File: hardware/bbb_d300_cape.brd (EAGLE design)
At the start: 58.4 x 54.6 mm, 38 parts, among them IC1 7414D, IC2 7414D, T1 2N3904, T2 2N3904, T3 2N3904, T4 2N3904, T5 2N3904

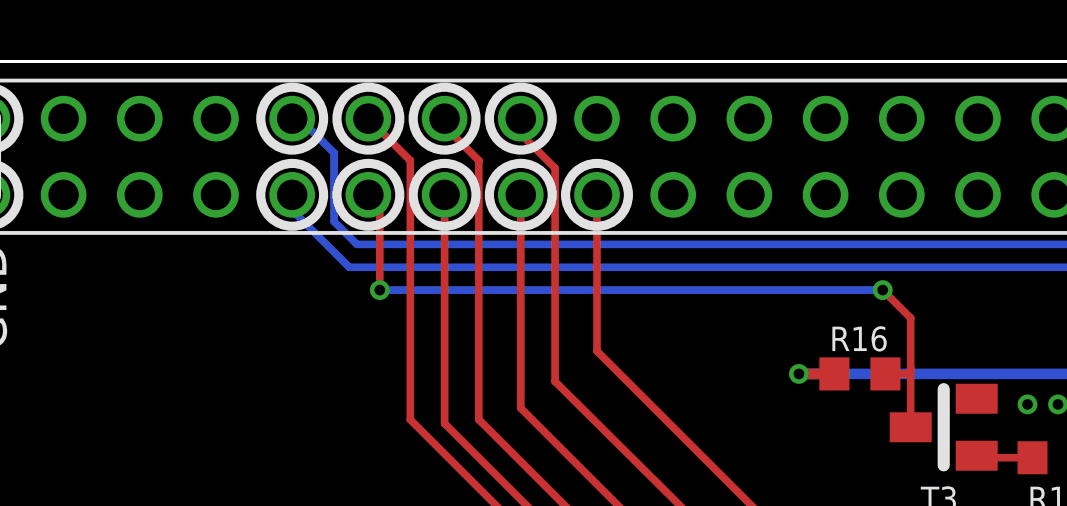
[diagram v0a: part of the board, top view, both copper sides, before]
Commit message: connect tool length to P8.08
Signed-off-by: Vladimir Pantelic <vladimir@pantelic.net>
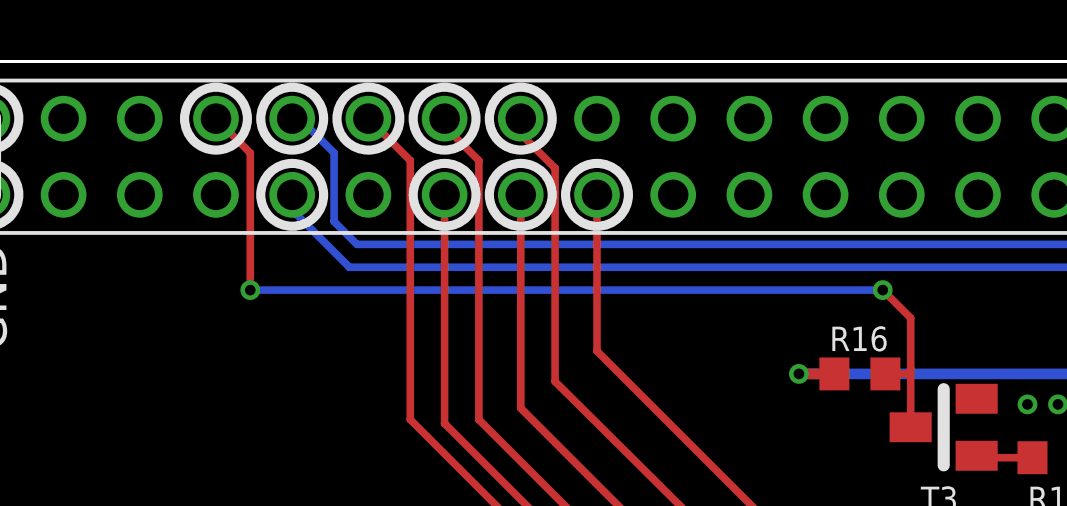
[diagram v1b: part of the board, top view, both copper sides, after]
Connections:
- net ERR3 renamed ERR3V3
- net HOME3 renamed HOME3V3
- removed net LENGTH3: PCB2.P8.11, R16.1, T3.C
- new net LENGTH3V3: PCB2.P8.8, R16.1, T3.C
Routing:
- net LENGTH3V3: track 0.00 -> 33.2 mm, vias 0 -> 2
- net LENGTH3: track 26.0 -> 0.00 mm, vias 2 -> 0
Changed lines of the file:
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@@
 <circle x="34.925" y="52.705" radius="1.04726875" width="0.3048" layer="21"/>
 <circle x="29.845" y="50.165" radius="1.04726875" width="0.3048" layer="21"/>
-<circle x="32.385" y="50.165" radius="1.04726875" width="0.3048" layer="21"/>
+<circle x="27.305" y="52.705" radius="1.04726875" width="0.3048" layer="21"/>
 <circle x="34.925" y="50.165" radius="1.04726875" width="0.3048" layer="21"/>
 <circle x="37.465" y="52.705" radius="1.04726875" width="0.3048" layer="21"/>
@@
 <wire x1="83.076" y1="38.1" x2="82.888" y2="37.912" width="0.254" layer="1"/>
 </signal>
-<signal name="ERR3">
+<signal name="ERR3V3">
 <contactref element="R4" pad="1"/>
 <contactref element="T2" pad="C"/>
@@
 <wire x1="84.494" y1="41.386" x2="84.412" y2="41.468" width="0.254" layer="1"/>
 </signal>
-<signal name="HOME3">
+<signal name="HOME3V3">
 <contactref element="R3" pad="1"/>
 <contactref element="T1" pad="C"/>
@@
 <wire x1="62.126" y1="41.402" x2="62.06" y2="41.468" width="0.254" layer="1"/>
 </signal>
-<signal name="LENGTH3">
+<signal name="LENGTH3V3">
 <contactref element="R16" pad="1"/>
 <contactref element="T3" pad="C"/>
@@
 <wire x1="49.618" y1="44.196" x2="50.378" y2="44.196" width="0.254" layer="1"/>
 <wire x1="50.378" y1="44.196" x2="50.462" y2="44.366" width="0.254" layer="1"/>
-<contactref element="PCB2" pad="P8.11"/>
-<wire x1="32.385" y1="50.165" x2="32.766" y2="49.784" width="0.254" layer="1"/>
-<wire x1="32.766" y1="49.784" x2="32.766" y2="46.99" width="0.254" layer="1"/>
-<via x="32.766" y="46.99" extent="1-16" drill="0.3556"/>
-<wire x1="32.766" y1="46.99" x2="49.53" y2="46.99" width="0.254" layer="16"/>
+<via x="28.448" y="46.99" extent="1-16" drill="0.3556"/>
+<wire x1="28.448" y1="46.99" x2="49.53" y2="46.99" width="0.254" layer="16"/>
 <via x="49.53" y="46.99" extent="1-16" drill="0.3556"/>
 <wire x1="49.53" y1="46.99" x2="50.462" y2="46.058" width="0.254" layer="1"/>
 <wire x1="50.462" y1="46.058" x2="50.462" y2="44.366" width="0.254" layer="1"/>
+<contactref element="PCB2" pad="P8.8"/>
+<wire x1="28.448" y1="46.99" x2="28.448" y2="51.562" width="0.254" layer="1"/>
+<wire x1="28.448" y1="51.562" x2="27.305" y2="52.705" width="0.254" layer="1"/>
 </signal>
 <signal name="IN5">
